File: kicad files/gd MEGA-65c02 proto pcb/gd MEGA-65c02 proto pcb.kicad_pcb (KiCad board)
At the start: 4 copper layers, 106.2 x 99.9 mm, 57 parts, among them J1 Pwr, J10 XY, J11 14M Enable, J12 RGB Bin, J2 CTRL2, J3 Addr_Main_Data, J4 CTRL1, J5 Slot_Maker, J6 Aux Data_La, J7 CLKS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

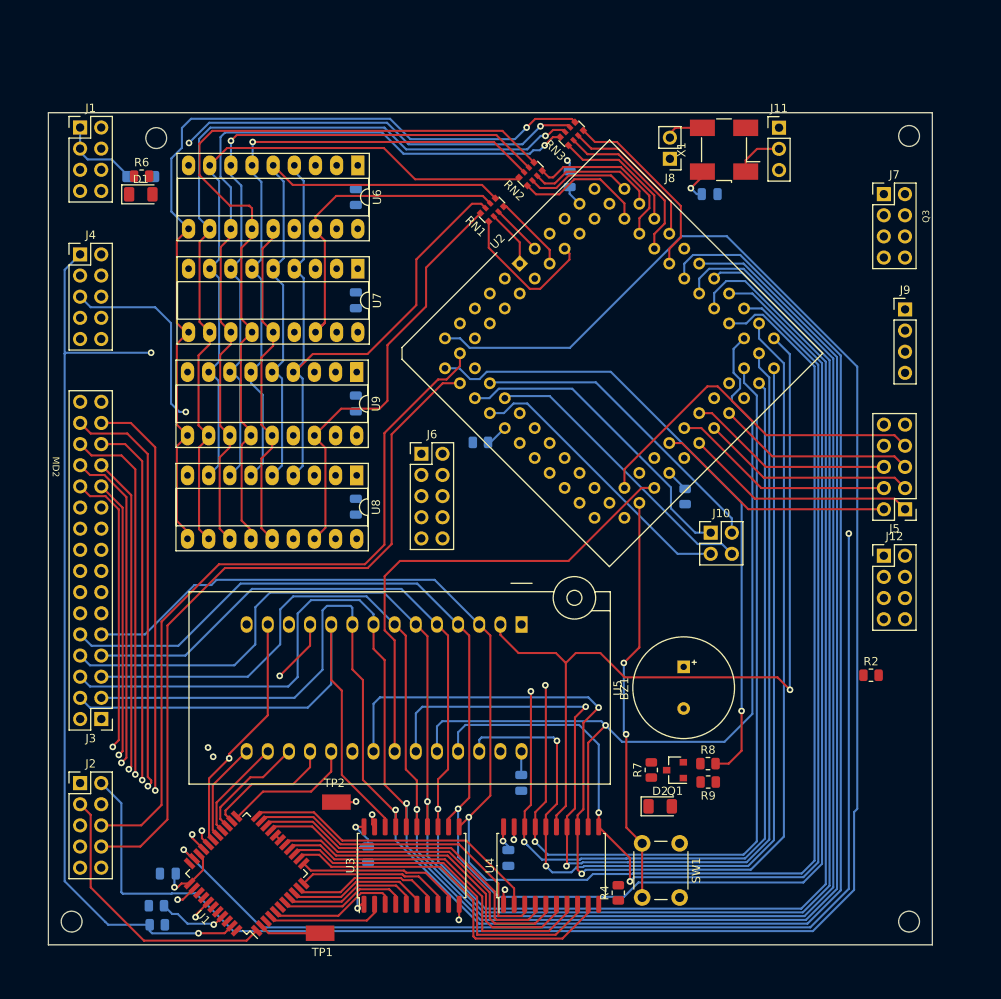
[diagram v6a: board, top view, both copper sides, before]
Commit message: 96 to go: adding power pours
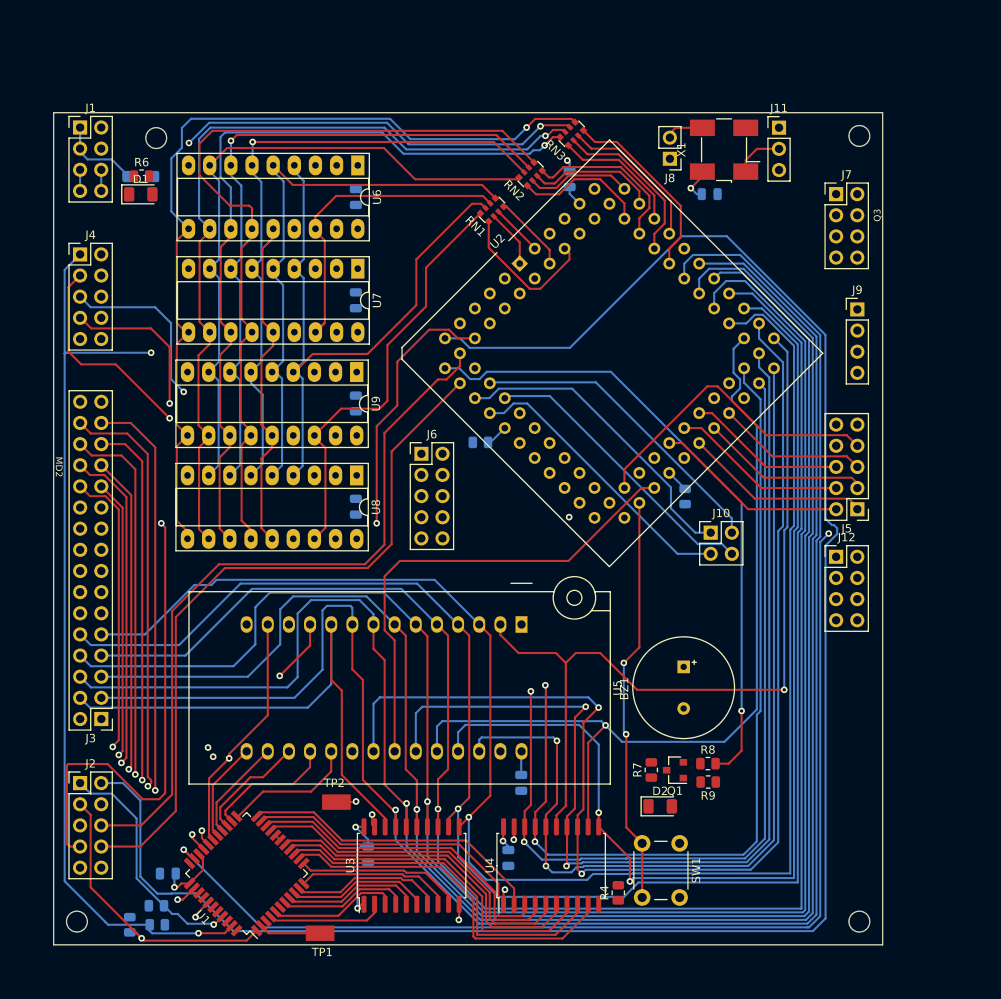
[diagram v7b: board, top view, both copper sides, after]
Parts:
- R2: moved to B.Cu
- moved R2 93.9 mm to (49.1, 142.1), turned to 270 degrees
- moved H2 5.97 mm to (136.8, 47.4)
- moved H4 5.97 mm to (136.8, 141.7)
- moved J12 5.73 mm to (134.0, 97.9)
- moved J5 5.73 mm to (136.5, 92.2)
- moved J9 5.73 mm to (136.5, 68.2)
- moved J7 5.73 mm to (134.0, 54.4)
- moved H1 0.63 mm to (42.8, 141.7)
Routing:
- net /~RESET: track 108.3 -> 251.2 mm, vias 3 -> 4
- net /PDLTRIG: track 0.00 -> 115.4 mm, vias 0 -> 2
- net /~DMA: track 22.7 -> 116.2 mm, vias 2 -> 3
- net /~INH: track 0.00 -> 83.3 mm, vias 0 -> 1
- net /~RDY: track 8.36 -> 28.8 mm
- net /RGB1: track 58.8 -> 47.1 mm
- net /RGB8: track 43.8 -> 38.0 mm
- net /S5: track 23.8 -> 18.1 mm
- net /S4: track 24.9 -> 19.1 mm
- net /S2: track 27.0 -> 21.2 mm
- net /S0: track 29.1 -> 23.3 mm
- net /Q3: track 122.3 -> 116.5 mm
- net /MDI-MDO: track 43.0 -> 37.3 mm
- net /CREF: track 117.7 -> 112.0 mm
- net /7M: track 117.8 -> 112.0 mm
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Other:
- board size 106.2 x 99.9 mm -> 99.6 x 99.9 mm

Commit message: 24 to go: After Zones
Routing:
- added copper zone on F.Cu, net +5V
- added copper zone on In2.Cu, net +5V
- added copper zone on B.Cu, net GND
- added copper zone on In1.Cu, net GND
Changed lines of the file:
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@@
   (segment (start 124.4854 48.9204) (end 127.127 48.9204) (width 0.25) (layer F.Cu) (net 131) (status 20))
   (segment (start 123.123 50.2828) (end 124.4854 48.9204) (width 0.25) (layer F.Cu) (net 131))
+  (zone (net 3) (net_name GND) (layer In1.Cu) (hatch edge 0.508)
+    (connect_pads (clearance 0.254))
+    (min_thickness 0.254)
+    (fill yes (arc_segments 32) (thermal_gap 0.254) (thermal_bridge_width 0.508))
+    (polygon
+      (pts
+        (xy 142.24 147.32) (xy 35.56 147.32) (xy 35.56 43.18) (xy 142.24 43.18)
+      )
+    )
+  )
+  (zone (net 3) (net_name GND) (layer B.Cu) (hatch edge 0.508)
+    (connect_pads (clearance 0.254))
+    (min_thickness 0.254)
+    (fill yes (arc_segments 32) (thermal_gap 0.254) (thermal_bridge_width 0.508))
+    (polygon
+      (pts
+        (xy 142.24 147.32) (xy 35.56 147.32) (xy 35.56 43.18) (xy 142.24 43.18)
+      )
+    )
+  )
+  (zone (net 2) (net_name +5V) (layer F.Cu) (hatch edge 0.508)
+    (connect_pads (clearance 0.254))
+    (min_thickness 0.254)
+    (fill yes (arc_segments 32) (thermal_gap 0.254) (thermal_bridge_width 0.508))
+    (polygon
+      (pts
+        (xy 142.24 147.32) (xy 35.56 147.32) (xy 35.56 43.18) (xy 142.24 43.18)
+      )
+    )
+  )
+  (zone (net 2) (net_name +5V) (layer In2.Cu) (hatch edge 0.508)
+    (connect_pads (clearance 0.254))
+    (min_thickness 0.254)
+    (fill yes (arc_segments 32) (thermal_gap 0.254) (thermal_bridge_width 0.508))
+    (polygon
+      (pts
+        (xy 142.24 147.32) (xy 35.56 147.32) (xy 35.56 43.18) (xy 142.24 43.18)
+      )
+    )
+  )
 )
